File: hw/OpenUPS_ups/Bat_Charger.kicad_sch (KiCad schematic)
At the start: 37 parts, among them Q601 2N7002, Q705 Q_NMOS_GDS, U402 NCP81151, U502 INA181A3, U503 MCP6001R, U504 MCP6001R

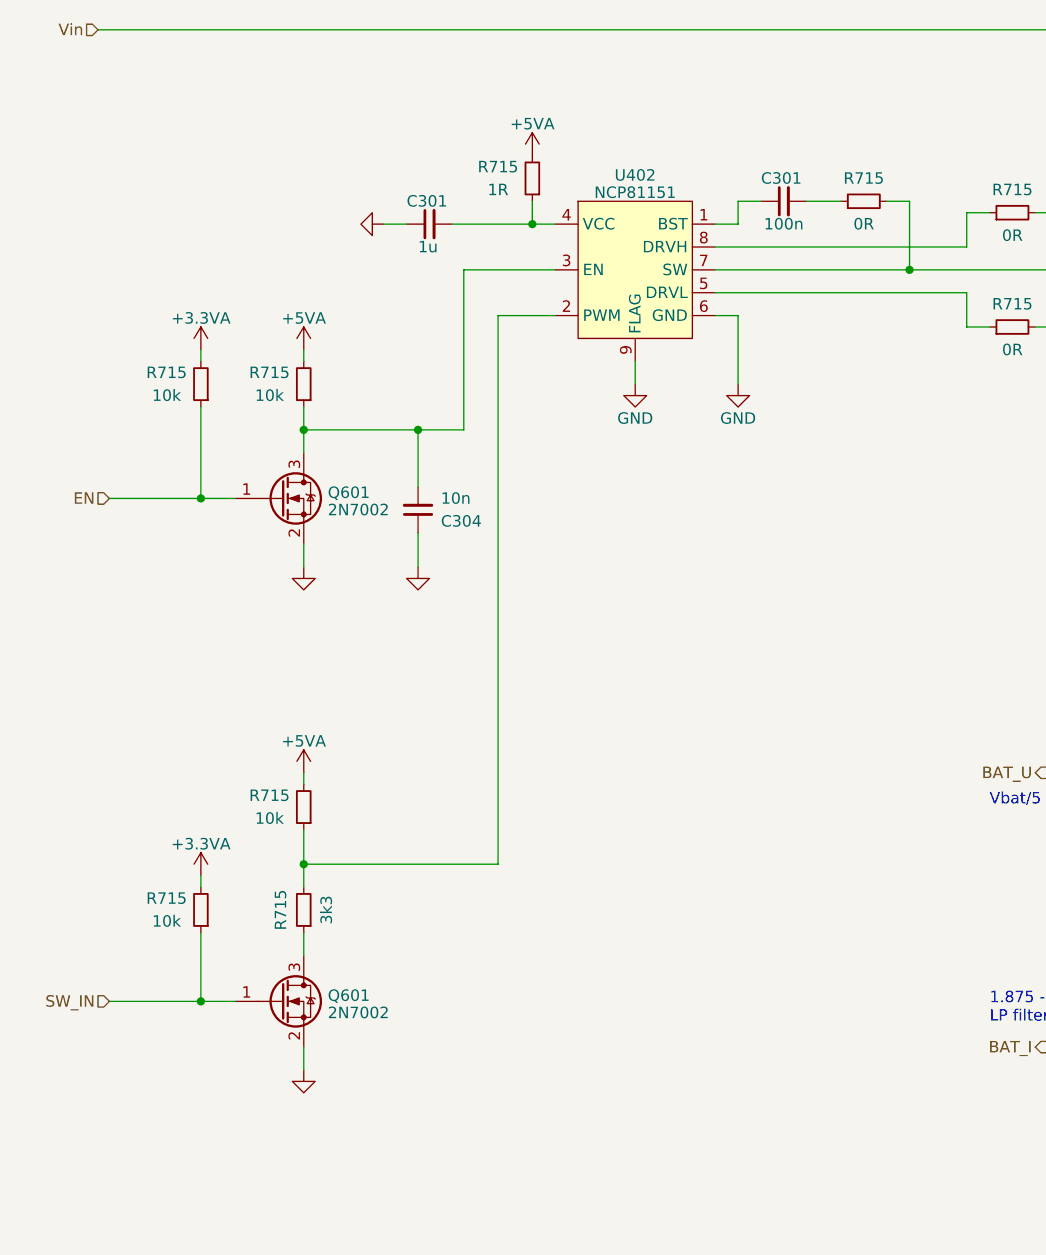
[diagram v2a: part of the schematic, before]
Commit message: Battery charger HB driver changed to NCP5901
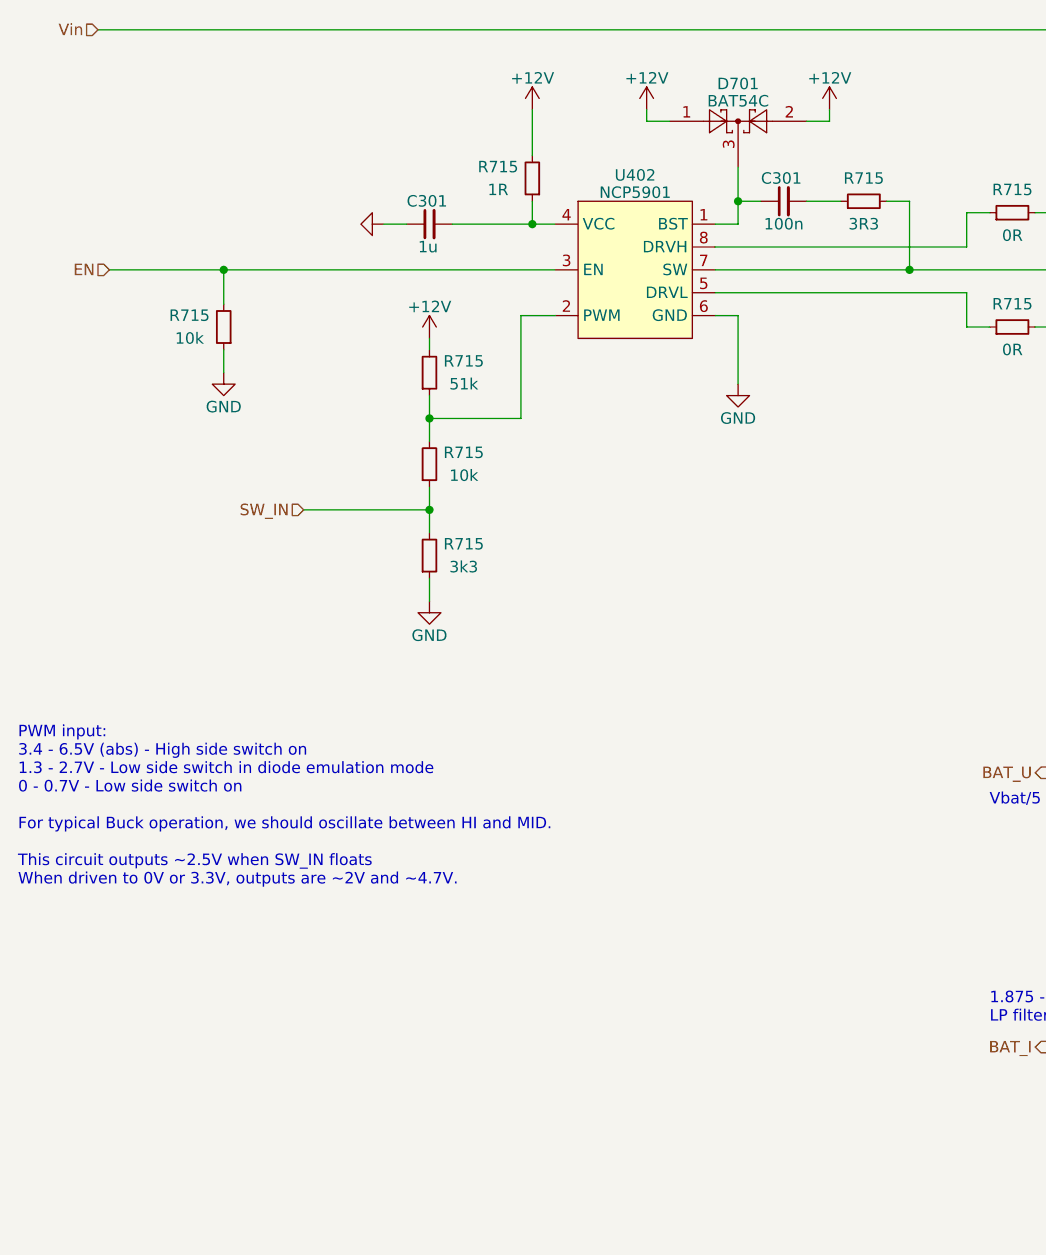
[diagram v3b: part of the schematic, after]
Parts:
- removed C304: 10n, Capacitor_SMD:C_0603_1608Metric, symbol Device:C_Small
- removed Q601 (x2): 2N7002, Package_TO_SOT_SMD:SOT-23, symbol Transistor_FET:2N7002
- removed R715 (x2): 10k, Resistor_SMD:R_0603_1608Metric, symbol Device:R_Small
- removed R715: 3k3, Resistor_SMD:R_0603_1608Metric, symbol Device:R_Small
- removed U402: NCP81151, Package_DFN_QFN:DFN-8-1EP_2x2mm_P0.5mm_EP0.9x1.3mm, symbol OpenUPS_ups:NCP81151
- added D701: BAT54C, Package_TO_SOT_SMD:SOT-23, symbol Diode:BAT54C
- added R715: 10k, Resistor_SMD:R_0603_1608Metric, symbol Device:R_Small
- added R715: 3k3, Resistor_SMD:R_0603_1608Metric, symbol Device:R_Small
- added U402: NCP5901, Package_SO:SOIC-8_3.9x4.9mm_P1.27mm, symbol OpenUPS_ups:NCP5901
- R715: value 10k -> 51k
- R715: value 0R -> 3R3
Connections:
- net +3.3VA: no longer R715.2
- net EN: now also R715.2, U402.3 (EN); no longer R715.1
- net GND: now also R715.1, R715.1, U402.6 (GND)
- net SW_IN: now also R715.1, R715.2
- net at C301.1: now also D701.3, U402.1 (BST)
- net at C301.2, R715.1: now also U402.4 (VCC)
- net at C715.1, L301.1, Q705.2 (D)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: now also U402.7 (SW)
- net at R715.1: now also U402.5 (DRVL)
- net at R715.1: now also U402.8 (DRVH)
- net at R715.1: now also R715.2, U402.2 (PWM)
- net +5VA renamed +12V
- net +12V: now also D701.1, D701.2
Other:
- note added: "PWM input: 3.4 - 6.5V (abs) - High side switch on 1.3 - 2.7V - Low side switch in diode emulation mode 0 - 0.7V - Low side switch on For typical Buck operation, we should oscillate between HI and MID. This circuit outputs ~2.5V when SW_IN floats When driven to 0V or 3.3V, outputs are ~2V and ~4.7V."
- moved on the sheet: R715

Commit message: 4th generation battery charger
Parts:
- removed C301: 100n, Capacitor_SMD:C_0603_1608Metric, symbol Device:C_Small
- removed C301: 1u, Capacitor_SMD:C_0603_1608Metric, symbol Device:C_Small
- removed C715: NM, Capacitor_SMD:C_0603_1608Metric, symbol Device:C_Small
- removed C724: 10u 35V, Capacitor_SMD:C_1206_3216Metric, symbol Device:C
- removed D701: BAT54C, Package_TO_SOT_SMD:SOT-23, symbol Diode:BAT54C
- removed Q705 (x2): Q_NMOS_GDS, Package_TO_SOT_SMD:TO-263-2, symbol Device:Q_NMOS_GDS
- removed R715 (x2): 10k, Resistor_SMD:R_0603_1608Metric, symbol Device:R_Small
- removed R715: NM, Resistor_SMD:R_0603_1608Metric, symbol Device:R_Small
- removed R715 (x2): 0R, Resistor_SMD:R_0603_1608Metric, symbol Device:R_Small
- removed R715: 1R, Resistor_SMD:R_0603_1608Metric, symbol Device:R_Small
- removed R715: 3k3, Resistor_SMD:R_0603_1608Metric, symbol Device:R_Small
- removed R715: 51k, Resistor_SMD:R_0603_1608Metric, symbol Device:R_Small
- removed R715: 3R3, Resistor_SMD:R_0603_1608Metric, symbol Device:R_Small
- removed U402: NCP5901, Package_SO:SOIC-8_3.9x4.9mm_P1.27mm, symbol OpenUPS_ups:NCP5901
- added C301 (x2): NM, Capacitor_SMD:C_0603_1608Metric, symbol Device:C_Small
- added C301: ADJ, Capacitor_SMD:C_0603_1608Metric, symbol Device:C_Small
- added C301, C?: 1u, Capacitor_SMD:C_0603_1608Metric, symbol Device:C_Small
- added C? (x2): 10u 35V, Capacitor_SMD:C_1206_3216Metric, symbol Device:C
- added C?: 10p, Capacitor_SMD:C_0603_1608Metric, symbol Device:C_Small
- added C?: 10u 50V, Capacitor_SMD:C_1206_3216Metric, symbol Device:C
- added C? (x2): 47u 35V, Capacitor_SMD:CP_Elec_6.3x7.7, symbol Device:C_Polarized
- added C?: 100n 35V, Capacitor_SMD:C_0603_1608Metric, symbol Device:C_Small
- added C?: 1n, Capacitor_SMD:C_0603_1608Metric, symbol Device:C_Small
- added D502: BAT54C, Package_TO_SOT_SMD:SOT-23, symbol Diode:BAT54C
- added D?: STPS20M100SG, Package_TO_SOT_SMD:TO-263-2, symbol Device:D_Schottky_AKA
- added L?: SRF1260-150M, Inductor_SMD:L_Bourns_SRF1260, symbol Device:L_Ferrite_Coupled_1243
- added Q?: Q_NMOS_GDS, Package_TO_SOT_SMD:TO-263-2, symbol Device:Q_NMOS_GDS
- added R715: 62k, Resistor_SMD:R_0603_1608Metric, symbol Device:R_Small
- added R715: 750R, Resistor_SMD:R_0603_1608Metric, symbol Device:R_Small
- added R715: 16k, Resistor_SMD:R_0603_1608Metric, symbol Device:R_Small
- added R?: 100m, Resistor_SMD:R_1206_3216Metric, symbol Device:R
- added R?: 3R3, Resistor_SMD:R_0603_1608Metric, symbol Device:R_Small
- added R?: 300R, Resistor_SMD:R_0603_1608Metric, symbol Device:R_Small
- added R?: ADJ, Resistor_SMD:R_0603_1608Metric, symbol Device:R_Small
- added R?: 3k6, Resistor_SMD:R_0603_1608Metric, symbol Device:R_Small
- added R?: NM, Resistor_SMD:R_0603_1608Metric, symbol Device:R_Small
- added U701: UC3845_SOIC8, Package_SO:SOIC-8_3.9x4.9mm_P1.27mm, symbol Regulator_Controller:UC3843_SOIC8
- L301: value SRP1038C-100M -> SRN4018-2R2M; footprint Inductor_SMD:L_Bourns_SRP1038C_10.0x10.0mm -> Inductor_SMD:L_Bourns-SRN4018; Comment 10u 8.5A -> 2u2 2.9A
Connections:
- net +12V: now also C301.2, U701.7 (VCC)
- net GND: now also C301.1, C?.2, C?.2, C?.2, C?.2, C?.2, C?.2, C?.2, C?.2, L?.1, R715.1, R715.1, R?.1, U701.5 (GND)
- net Vin: now also C301.1, C?.1, C?.1, C?.1, L?.4
- net at L301.1: now also C?.1, C?.1, D?.2 (K), R715.2
- new net: Q?.3 (S), R?.1, R?.2
- new net: C301.2, R715.1, R715.2, R?.1, U701.2 (FB)
- new net: Q?.1 (G), R?.1
- new net: R?.2, U701.6 (OUT)
- new net: C301.1, C301.1, D502.1, U701.1 (COMP)
- new net: C?.1, R?.1, U701.8 (VREF)
- new net: C301.2, R?.2 (x2)
- new net: C?.1, L?.3, Q?.2 (D), R?.1
- new net: C?.2, D?.1 (A), D?.3 (A), L?.2
- new net: C?.1, R?.2, U701.4 (RC)
- new net CS: C?.1, R?.2, U701.3 (CS)
- new net DAC: D502.3, R715.2
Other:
- note added: "0V keeps the converter off 1.3-2.5V range set current limits Actual output voltage must be monitored and regulated externally"
- note added: "> 40V!"
- note added: "Also applicable: UC1845 UC2845"
- note added: "Or BAT54S, BAT54"
- note added: "TODO: Make sure AVR DAC can source 3mA Otherwise add buffer Or change disabling method"
- note added: "This resistor keeps the charger off when DAC input is floating"
- note added: "Vds >= 40V"
- note removed: "PWM input: 3.4 - 6.5V (abs) - High side switch on 1.3 - 2.7V - Low side switch in diode emulation mode 0 - 0.7V - Low side switch on For typical Buck operation, we should oscillate between HI and MID. This circuit outputs ~2.5V when SW_IN floats When driven to 0V or 3.3V, outputs are ~2V and ~4.7V."
- note removed: "TODO: Find suitable NMOS"
- moved on the sheet: C301, C304, L301, R704, R715, U502, U503, U504

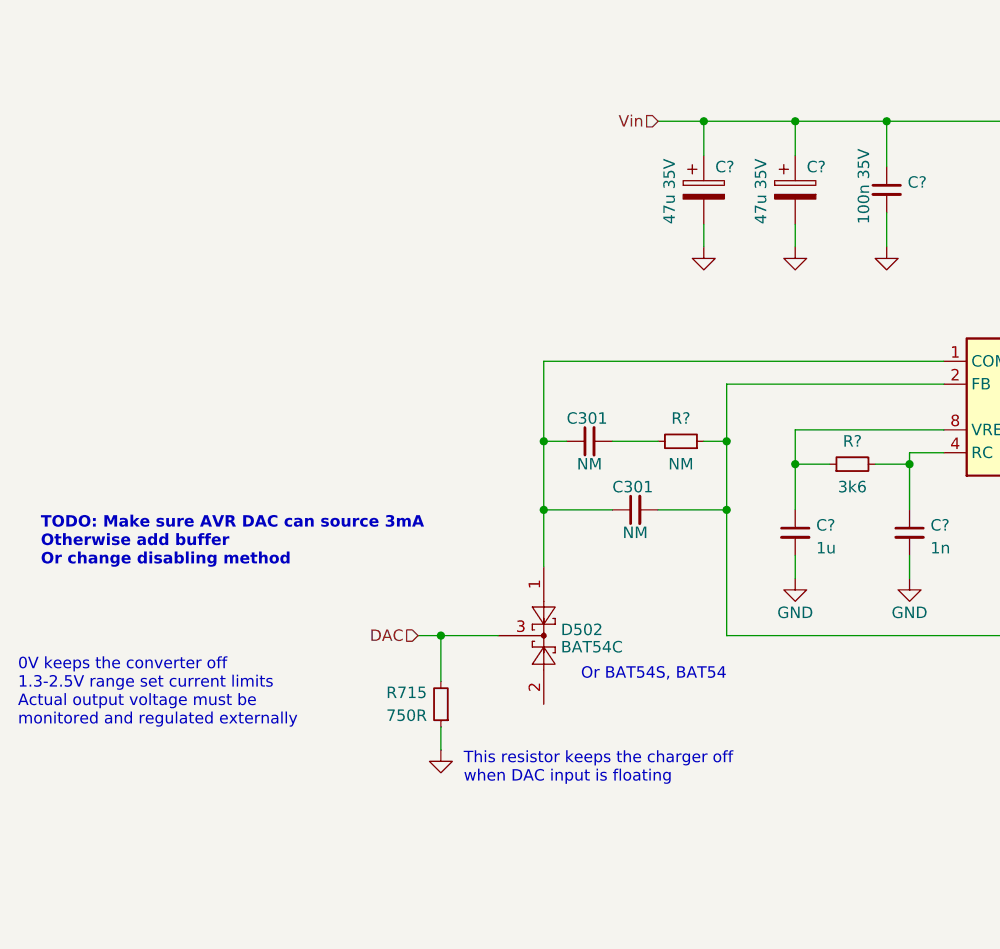
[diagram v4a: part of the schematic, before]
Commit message: External I2C isolator
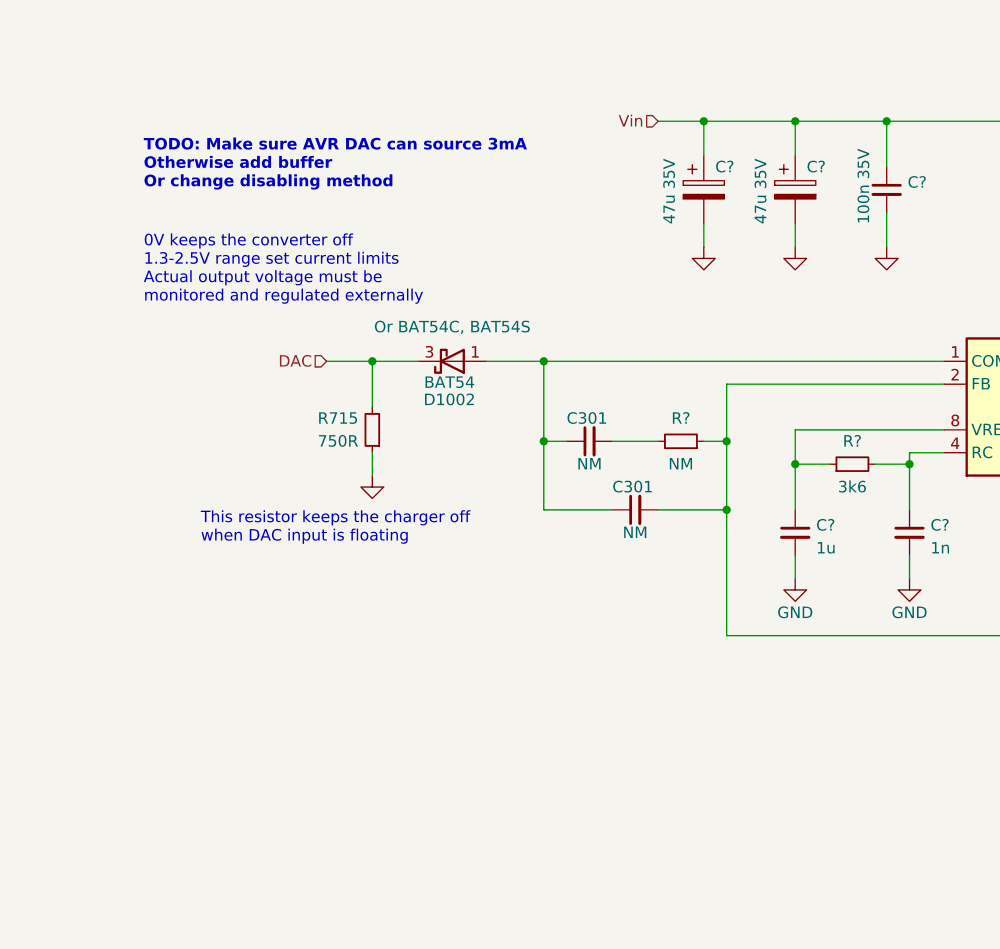
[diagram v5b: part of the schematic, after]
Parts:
- removed D502: BAT54C, Package_TO_SOT_SMD:SOT-23, symbol Diode:BAT54C
- added D1002: BAT54, Package_TO_SOT_SMD:SOT-23, symbol Diode:BAT54W
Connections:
- net DAC: now also D1002.3 (K)
- net at C301.1, C301.1, U701.1 (COMP): now also D1002.1 (A)
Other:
- note removed: "Or BAT54S, BAT54"
- moved on the sheet: R715

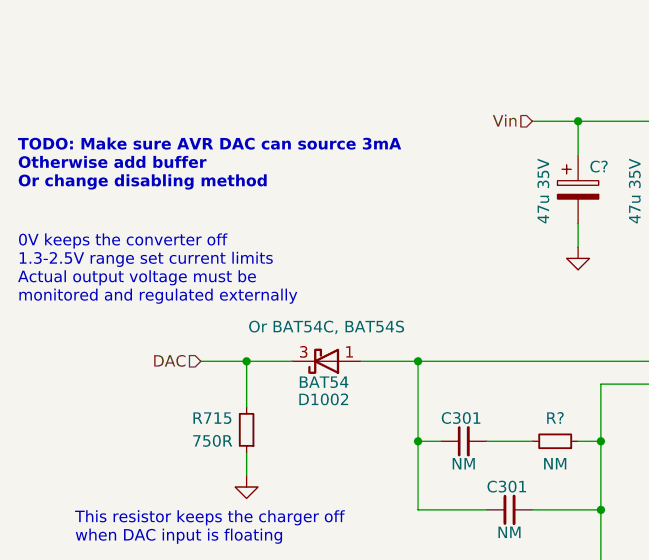
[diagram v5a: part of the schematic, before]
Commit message: Work on 5V; EN pins taken care of.
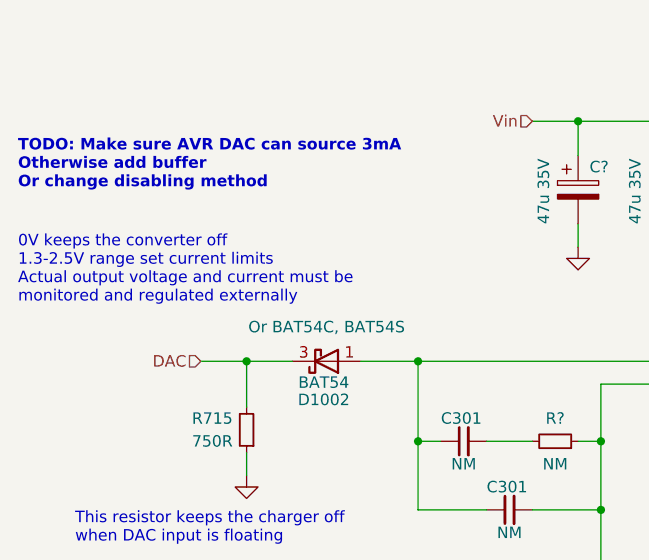
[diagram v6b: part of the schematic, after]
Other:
- note added: "0V keeps the converter off 1.3-2.5V range set current limits Actual output voltage and current must be monitored and regulated externally"
- note removed: "0V keeps the converter off 1.3-2.5V range set current limits Actual output voltage must be monitored and regulated externally"
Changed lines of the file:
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@@
     (effects (font (size 1.27 1.27)) (justify left bottom))
   )
-  (text "0V keeps the converter off\n1.3-2.5V range set current limits\nActual output voltage must be \nmonitored and regulated externally"
+  (text "0V keeps the converter off\n1.3-2.5V range set current limits\nActual output voltage and current must be \nmonitored and regulated externally"
     (at 31.75 55.88 0)
     (effects (font (size 1.27 1.27)) (justify left bottom))
@@
         )
         (path "/f77faec3-eac4-47f3-a2de-ec4a039f4502/0bd99307-a15c-41e8-997b-077d576f806c"
-          (reference "R?") (unit 1)
+          (reference "R430") (unit 1)
         )
       )
@@
         )
         (path "/f77faec3-eac4-47f3-a2de-ec4a039f4502/0bd99307-a15c-41e8-997b-077d576f806c"
-          (reference "C?") (unit 1)
+          (reference "C439") (unit 1)
         )
       )
@@
         )
         (path "/f77faec3-eac4-47f3-a2de-ec4a039f4502/0bd99307-a15c-41e8-997b-077d576f806c"
-          (reference "C?") (unit 1)
+          (reference "C437") (unit 1)
         )
       )
@@
         )
         (path "/f77faec3-eac4-47f3-a2de-ec4a039f4502/0bd99307-a15c-41e8-997b-077d576f806c"
-          (reference "C?") (unit 1)
+          (reference "C438") (unit 1)
         )
       )
@@
         )
         (path "/f77faec3-eac4-47f3-a2de-ec4a039f4502/0bd99307-a15c-41e8-997b-077d576f806c"
-          (reference "C?") (unit 1)
+          (reference "C429") (unit 1)
         )
       )
@@
         )
         (path "/f77faec3-eac4-47f3-a2de-ec4a039f4502/0bd99307-a15c-41e8-997b-077d576f806c"
-          (reference "Q?") (unit 1)
+          (reference "Q405") (unit 1)
         )
       )
@@
         )
         (path "/f77faec3-eac4-47f3-a2de-ec4a039f4502/0bd99307-a15c-41e8-997b-077d576f806c"
-          (reference "C?") (unit 1)
+          (reference "C440") (unit 1)
         )
       )
@@
         )
         (path "/f77faec3-eac4-47f3-a2de-ec4a039f4502/0bd99307-a15c-41e8-997b-077d576f806c"
-          (reference "D?") (unit 1)
+          (reference "D403") (unit 1)
         )
       )
@@
         )
         (path "/f77faec3-eac4-47f3-a2de-ec4a039f4502/0bd99307-a15c-41e8-997b-077d576f806c"
-          (reference "C?") (unit 1)
+          (reference "C436") (unit 1)
         )
       )
@@
         )
         (path "/f77faec3-eac4-47f3-a2de-ec4a039f4502/0bd99307-a15c-41e8-997b-077d576f806c"
-          (reference "R?") (unit 1)
+          (reference "R429") (unit 1)
         )
       )
@@
         )
         (path "/f77faec3-eac4-47f3-a2de-ec4a039f4502/0bd99307-a15c-41e8-997b-077d576f806c"
-          (reference "L?") (unit 1)
+          (reference "L402") (unit 1)
         )
       )
@@
         )
         (path "/f77faec3-eac4-47f3-a2de-ec4a039f4502/0bd99307-a15c-41e8-997b-077d576f806c"
-          (reference "C?") (unit 1)
+          (reference "C430") (unit 1)
         )
       )
@@
         )
         (path "/f77faec3-eac4-47f3-a2de-ec4a039f4502/0bd99307-a15c-41e8-997b-077d576f806c"
-          (reference "R?") (unit 1)
-        )
-      )
+          (reference "R428") (unit 1)
+        )
+      )
